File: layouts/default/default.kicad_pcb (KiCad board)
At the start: 2 copper layers, 9 parts

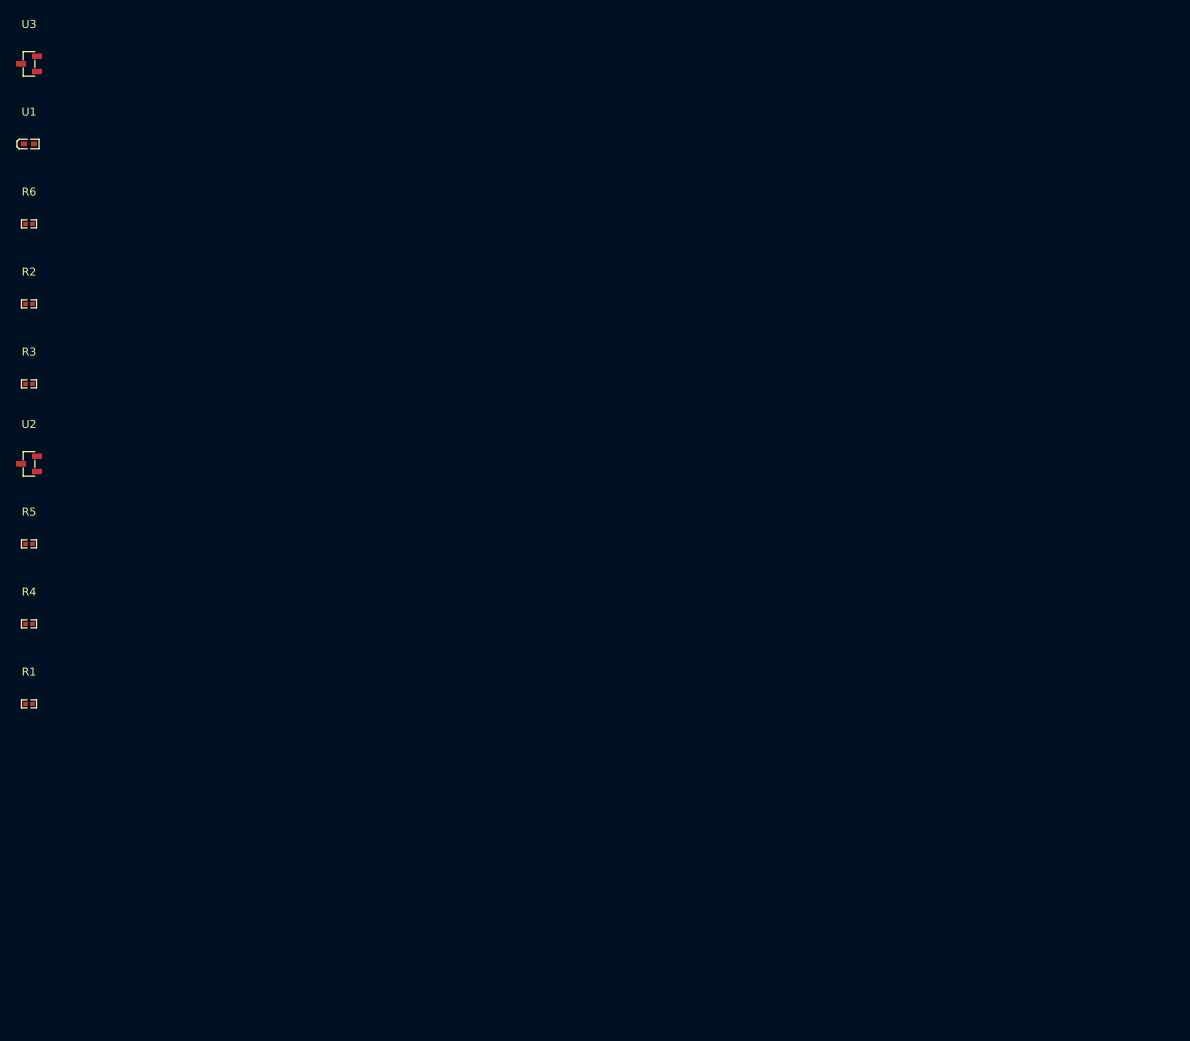
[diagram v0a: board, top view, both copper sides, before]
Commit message: fixed PCB layout + ci.yml
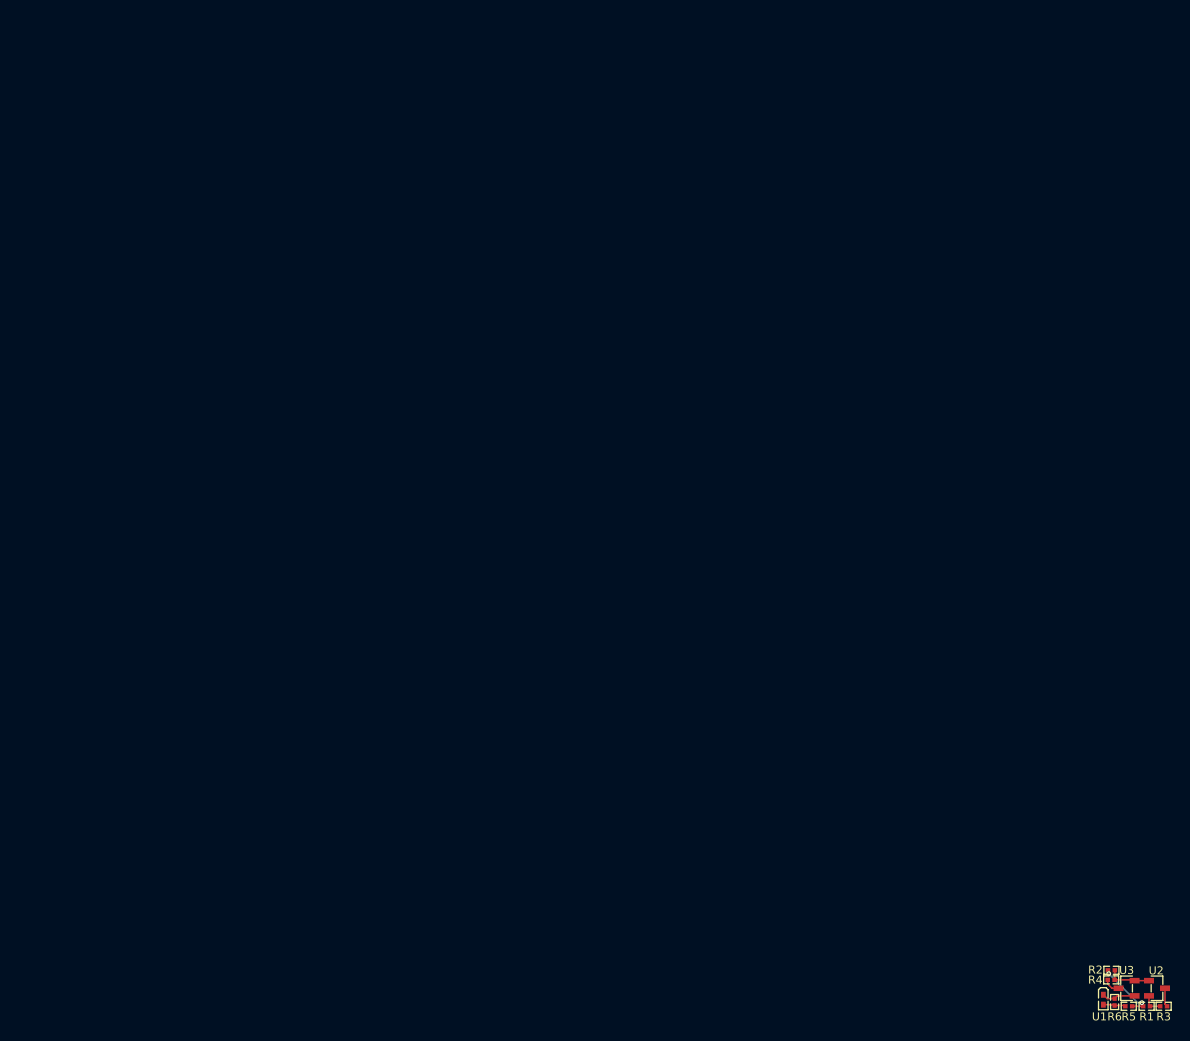
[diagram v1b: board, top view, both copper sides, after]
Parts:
- moved U3 179.4 mm to (137.2, 35.5)
- moved U1 171.7 mm to (134.3, 37.0), turned to -90 degrees
- moved R6 167.0 mm to (135.7, 37.3), turned to 90 degrees
- moved R3 161.8 mm to (141.8, 37.8)
- moved R2 158.9 mm to (135.3, 33.3)
- moved U2 155.5 mm to (141.0, 35.5), turned to 180 degrees
- moved R5 149.1 mm to (137.5, 37.8), turned to 180 degrees
- moved R1 144.7 mm to (139.7, 37.8)
- moved R4 142.4 mm to (135.3, 34.5), turned to 180 degrees
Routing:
- net hv: track 0.00 -> 7.80 mm, vias 0 -> 2
- net REF: track 0.00 -> 5.55 mm
- net OUT: track 0.00 -> 4.24 mm
- net anode: track 0.00 -> 2.82 mm
- net REF-1: track 0.00 -> 2.62 mm
- net A: track 0.00 -> 2.36 mm
- net gnd: track 0.00 -> 2.10 mm

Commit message: removed to version
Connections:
- R1 pad 2: REF-1 -> REF
- R2 pad 2: REF -> K
- R3 pad 1: REF-1 -> REF
- R4 pad 1: REF -> K
- U2 pad 1: REF -> K
- U2 pad 2: REF-1 -> REF
- U3 pad 2: REF -> K
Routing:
- net K: track 0.00 -> 5.55 mm
- net REF: track 5.55 -> 2.62 mm
- net REF-1: track 2.62 -> 0.00 mm
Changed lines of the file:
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@@
 	)
 	(net 0 "")
-	(net 1 "REF")
+	(net 1 "K")
 	(net 2 "OUT")
-	(net 3 "REF-1")
+	(net 3 "REF")
 	(net 4 "hv")
 	(net 5 "gnd")
@@
 			(size 0.57 0.54)
 			(layers "F.Cu" "F.Mask" "F.Paste")
-			(net 3 "REF-1")
+			(net 3 "REF")
 		)
 		(pad "2" smd rect
@@
 			(size 1.25 0.7)
 			(layers "F.Cu" "F.Mask" "F.Paste")
-			(net 1 "REF")
+			(net 1 "K")
 		)
 		(pad "3" smd rect
@@
 			(size 0.57 0.54)
 			(layers "F.Cu" "F.Mask" "F.Paste")
-			(net 1 "REF")
+			(net 1 "K")
 		)
 		(pad "2" smd rect
@@
 			(size 0.57 0.54)
 			(layers "F.Cu" "F.Mask" "F.Paste")
-			(net 3 "REF-1")
+			(net 3 "REF")
 		)
 		(embedded_fonts no)
@@
 			(size 0.57 0.54)
 			(layers "F.Cu" "F.Mask" "F.Paste")
-			(net 1 "REF")
+			(net 1 "K")
 		)
 		(embedded_fonts no)
@@
 			(size 1.25 0.7)
 			(layers "F.Cu" "F.Mask" "F.Paste")
-			(net 1 "REF")
+			(net 1 "K")
 		)
 		(pad "2" smd rect
@@
 			(size 1.25 0.7)
 			(layers "F.Cu" "F.Mask" "F.Paste")
-			(net 3 "REF-1")
+			(net 3 "REF")
 		)
 		(pad "3" smd rect
